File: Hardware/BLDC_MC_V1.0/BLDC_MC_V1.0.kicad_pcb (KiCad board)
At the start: 8 copper layers, 120 x 55 mm, 227 parts, among them J3 USB_C_Receptacle_USB2.0_16P, J4 Conn_02x03_Counter_Clockwise, J5 S6B-PH-K-S_LF__SN_, J6 XT60-M, J7 1714984, J8 S10B-PHDSS LFSN, Q1 BSC027N10NS5ATMA1, Q2 BSC027N10NS5ATMA1, Q3 BSC027N10NS5ATMA1, Q4 BSC027N10NS5ATMA1, Q5 BSC027N10NS5ATMA1, Q6 BSC027N10NS5ATMA1, Q7 BSC027N10NS5ATMA1, SW1 SW_Push, U1 LM76005RNPR, U10 TLV9061IDBVR, U11 TLV9061IDBVR, U12 TLV9061IDBVR, U13 TLV9061IDBVR, U14 TLV9061IDBVR, U15 TLV9061IDBVR, U16 LM74700QDRQ1, U2 TCAN334DR, U3 TLV9061IDBVR, U4 STM32G431RBT6, U5 LDL1117S33R, U6 DRV8353HRTAR, U7 NCV4274ADT50RKG, U8 25LC256-E_SN, U9 USBLC6-2SC6, Y1 7M-24.000MAAJ-T, Y2 ABS07-32.768KHZ-T

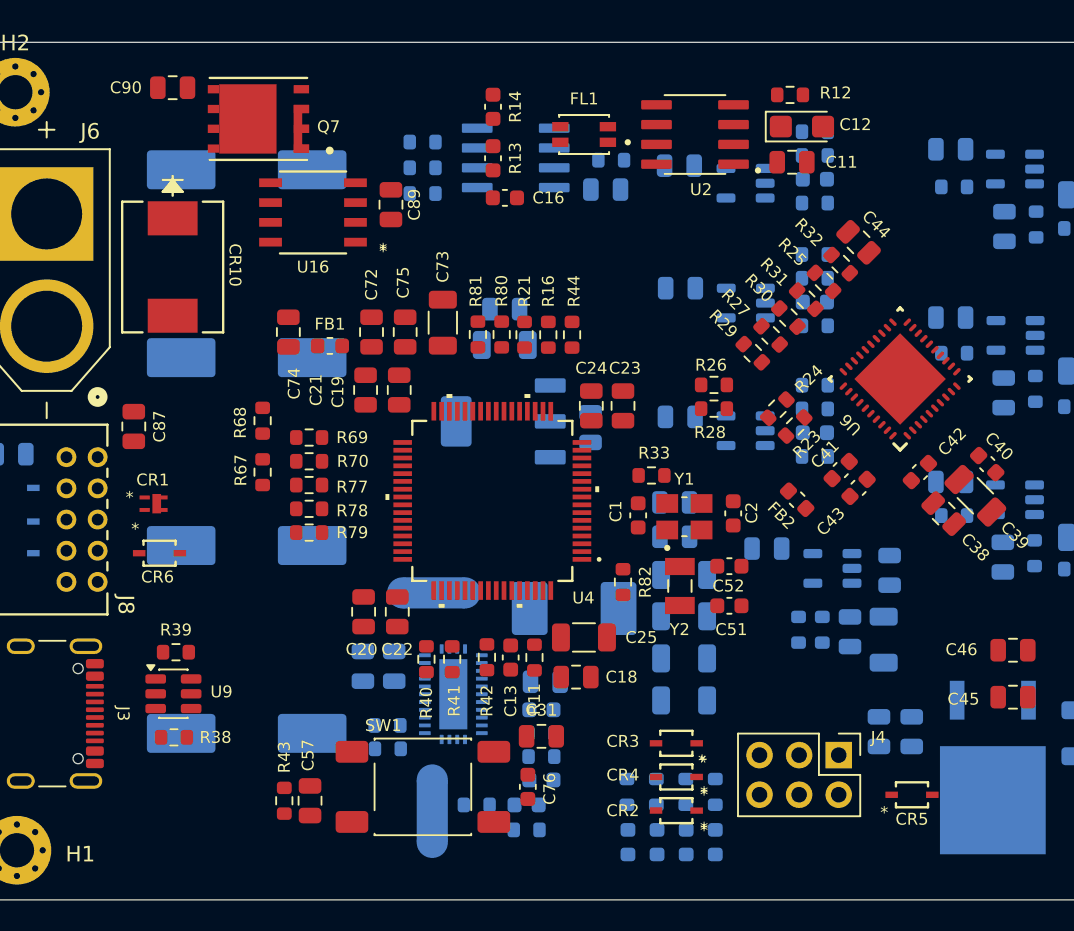
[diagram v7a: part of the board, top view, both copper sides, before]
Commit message: Add Stackup for the PCB and define the control impedance traces
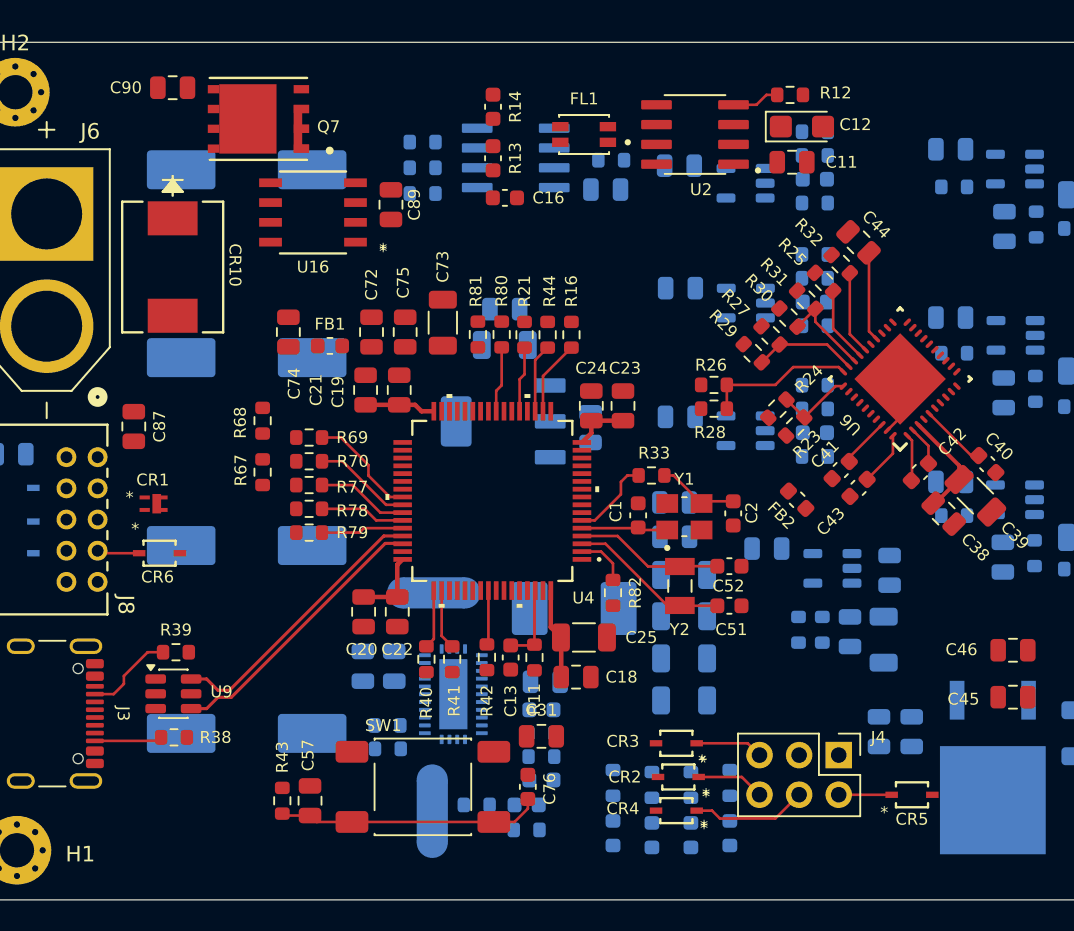
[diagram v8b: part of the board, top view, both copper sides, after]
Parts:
- moved CR2 2.16 mm to (82.9, 60.7)
- moved CR4 2.16 mm to (82.8, 62.9)
- moved R44 1.57 mm to (74.5, 32.3)
- moved R16 1.48 mm to (76.1, 32.3)
- moved D1 1.12 mm to (78.7, 64.3)
- moved D3 1.10 mm to (86.2, 64.3)
- moved R35 1.10 mm to (86.2, 61.1)
- moved R37 1.06 mm to (78.7, 61.1)
- moved R82 0.94 mm to (78.7, 48.9)
- moved D2 0.56 mm to (81.2, 64.4)
- moved R36 0.55 mm to (83.7, 61.2)
- moved D4 0.54 mm to (83.7, 64.4)
- moved R34 0.53 mm to (81.2, 61.2)
- moved R43 0.13 mm to (57.5, 62.2)
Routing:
- net +3.3V: track 0.00 -> 24.5 mm
- net /BLDC_MC_V1.0_MCU/NRST: track 0.00 -> 20.2 mm
- net /BLDC_MC_V1.0_MCU/USB_P: track 0.00 -> 18.0 mm
- net /BLDC_MC_V1.0_MCU/USB_N: track 0.00 -> 18.0 mm
- net Net-(U4-PC14): track 0.00 -> 10.3 mm
- net Net-(U6-GAIN): track 0.00 -> 9.60 mm
- net Net-(U4-PC15): track 0.00 -> 9.50 mm
- net Net-(J4-Pin_4): track 0.00 -> 7.41 mm
- net Net-(U4-PC8): track 0.00 -> 7.15 mm
- net +12V: track 0.00 -> 6.89 mm
- net Net-(U6-VDS): track 0.00 -> 6.63 mm
- net Net-(U4-PC9): track 0.00 -> 6.33 mm
- net /BLDC_MC_V1.0_Gate_Drive/IDRIVE: track 0.00 -> 5.98 mm
- net Net-(U4-PA8): track 0.00 -> 5.90 mm
- net Net-(J3-CC1): track 0.00 -> 5.78 mm
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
